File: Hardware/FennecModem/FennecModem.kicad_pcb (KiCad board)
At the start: 2 copper layers, 70 x 116.7 mm, 15 parts, among them J101 USB_C_Receptacle_USB2.0, J201 Conn_Coaxial, U101 ATmega32U4-A, U201 DRA818V

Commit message: Add more
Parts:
- moved FL201 83.8 mm to (150.5, 52.5), turned to 90 degrees
- moved J201 57.1 mm to (150.5, 42.9), turned to 90 degrees
- moved U201 49.2 mm to (164.0, 69.5), turned to -90 degrees
- moved J101 38.9 mm to (128.0, 45.0), turned to 180 degrees
- moved R204 37.8 mm to (151.0, 98.4)
- moved JP201 24.4 mm to (150.3, 84.0), turned to -90 degrees
- moved U101 14.3 mm to (151.0, 126.0), turned to 45 degrees
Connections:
- C101 pad 1: unconnected-(C101-Pad1) -> +5V
- C101 pad 15: unconnected-(C101-Pad15) -> GND
- C101 pad 16: unconnected-(C101-Pad16) -> +12V
- C101 pad 30: unconnected-(C101-Pad30) -> GND
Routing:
- net GND: track 0.00 -> 9.28 mm, vias 0 -> 35
- added copper zone on B.Cu, net GND
- added copper zone on F.Cu, net GND

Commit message: Bump kenwoodfox libs
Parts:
- moved J101 0.62 mm to (128.0, 44.4)
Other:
- board size 70 x 116.7 mm -> 75 x 116.7 mm

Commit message: Bump upstream libs with new logo
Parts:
- added G***: LOGO, KenwoodFox:fennec_logo, F.Cu at (174.5, 133.5)
- added G***: LOGO, KenwoodFox:fennec_logo, B.Cu at (125.0, 61.8)
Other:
- board text added: "F.E.N.N.E.C. MODEM"

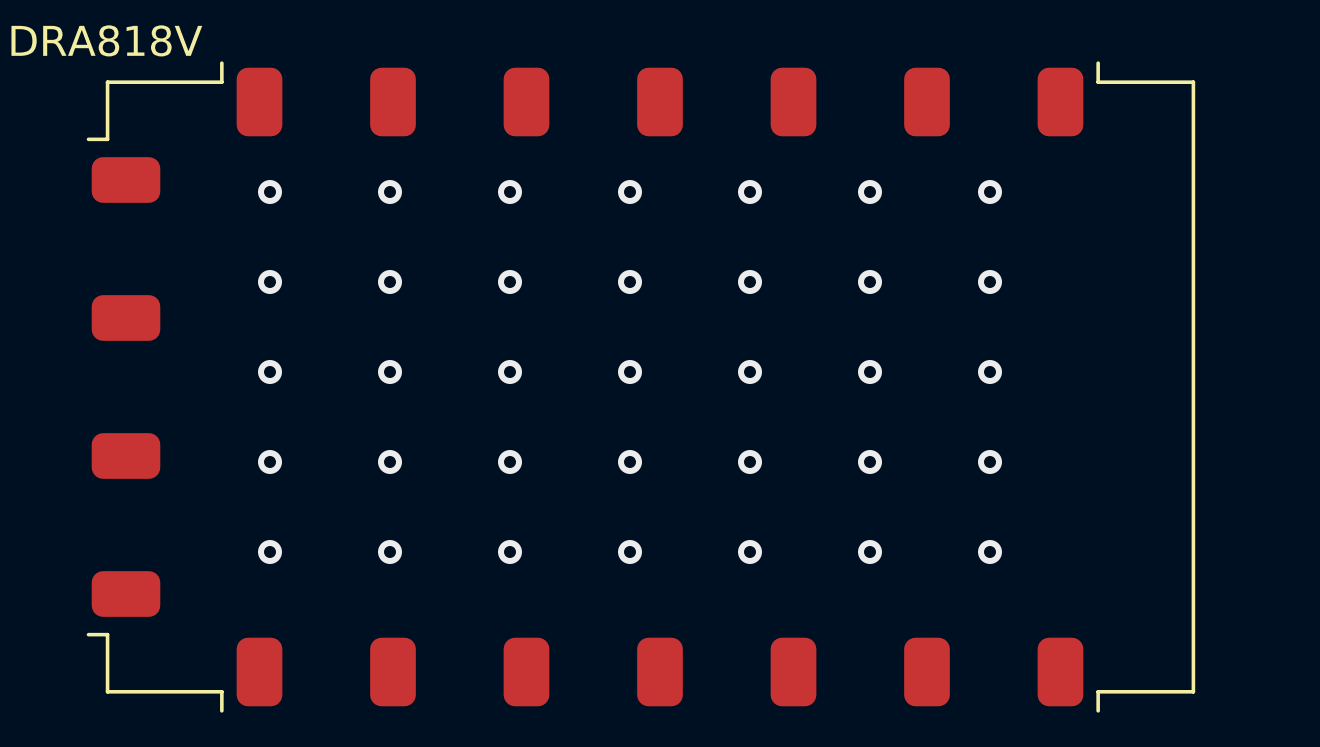
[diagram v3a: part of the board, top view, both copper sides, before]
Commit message: Bump kicad libs and add thermal holes to board
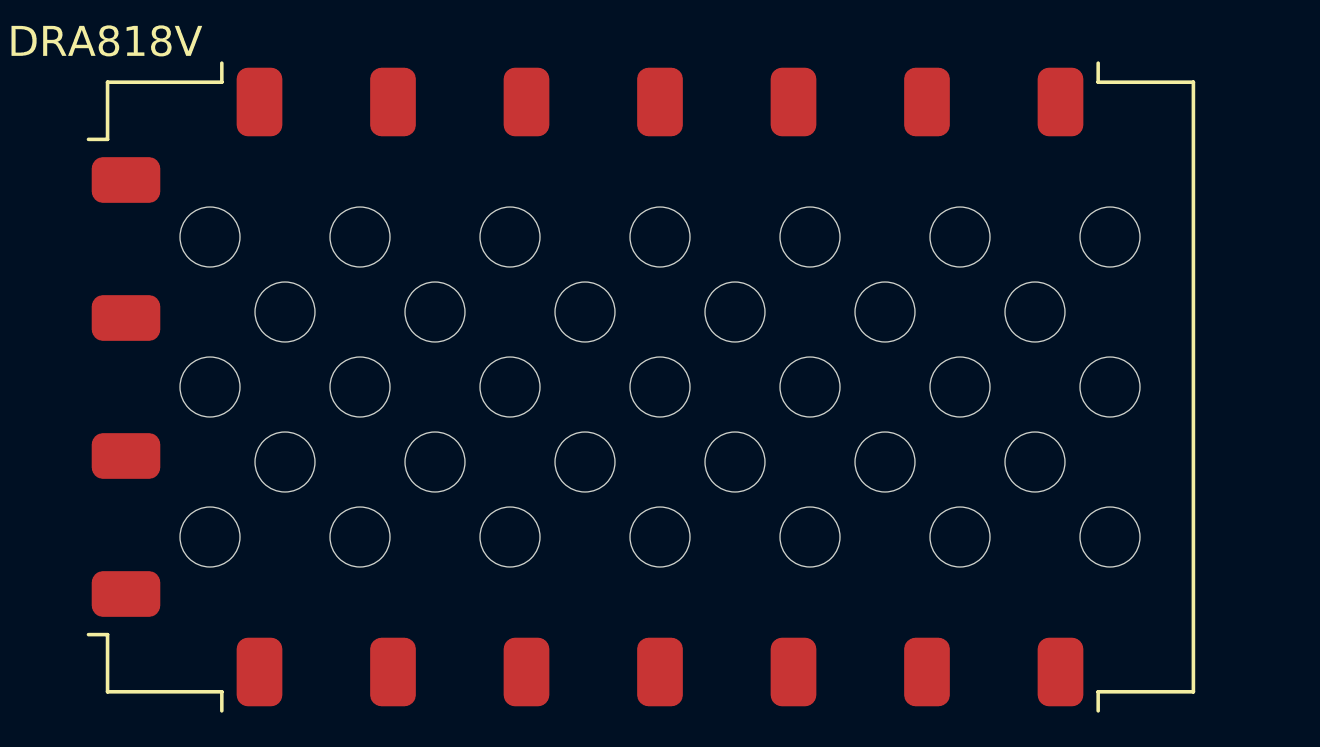
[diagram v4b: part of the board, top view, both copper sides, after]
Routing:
- net GND: vias 35 -> 0
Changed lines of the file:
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@@
         (effects (font (size 1 1) (thickness 0.15)))
     )
-    (fp_text user "${REFERENCE}" (at 0 0 unlocked) (layer "F.Fab")
+    (fp_text user "${REFERENCE}" (at 8.255 20.955 -90 unlocked) (layer "F.Fab")
         (effects (font (size 1 1) (thickness 0.15)))
     )
@@
     (fp_rect (start -9.525 -17.78) (end 9.525 17.78)
       (stroke (width 0.12) (type solid)) (fill none) (layer "F.Fab"))
+    (pad "" np_thru_hole circle (at -5 -15 270) (size 2 2) (drill 2) (layers "F&B.Cu" "*.Mask"))
+    (pad "" np_thru_hole circle (at -5 -10 270) (size 2 2) (drill 2) (layers "F&B.Cu" "*.Mask"))
+    (pad "" np_thru_hole circle (at -5 -5 270) (size 2 2) (drill 2) (layers "F&B.Cu" "*.Mask"))
+    (pad "" np_thru_hole circle (at -5 0 270) (size 2 2) (drill 2) (layers "F&B.Cu" "*.Mask"))
+    (pad "" np_thru_hole circle (at -5 5 270) (size 2 2) (drill 2) (layers "F&B.Cu" "*.Mask"))
+    (pad "" np_thru_hole circle (at -5 10 270) (size 2 2) (drill 2) (layers "F&B.Cu" "*.Mask"))
+    (pad "" np_thru_hole circle (at -5 15 270) (size 2 2) (drill 2) (layers "F&B.Cu" "*.Mask"))
+    (pad "" np_thru_hole circle (at -2.5 -12.5 270) (size 2 2) (drill 2) (layers "F&B.Cu" "*.Mask"))
+    (pad "" np_thru_hole circle (at -2.5 -7.5 270) (size 2 2) (drill 2) (layers "F&B.Cu" "*.Mask"))
+    (pad "" np_thru_hole circle (at -2.5 -2.5 270) (size 2 2) (drill 2) (layers "F&B.Cu" "*.Mask"))
+    (pad "" np_thru_hole circle (at -2.5 2.5 270) (size 2 2) (drill 2) (layers "F&B.Cu" "*.Mask"))
+    (pad "" np_thru_hole circle (at -2.5 7.5 270) (size 2 2) (drill 2) (layers "F&B.Cu" "*.Mask"))
+    (pad "" np_thru_hole circle (at -2.5 12.5 270) (size 2 2) (drill 2) (layers "F&B.Cu" "*.Mask"))
+    (pad "" np_thru_hole circle (at 0 -15 270) (size 2 2) (drill 2) (layers "F&B.Cu" "*.Mask"))
+    (pad "" np_thru_hole circle (at 0 -10 270) (size 2 2) (drill 2) (layers "F&B.Cu" "*.Mask"))
+    (pad "" np_thru_hole circle (at 0 -5 270) (size 2 2) (drill 2) (layers "F&B.Cu" "*.Mask"))
+    (pad "" np_thru_hole circle (at 0 0 270) (size 2 2) (drill 2) (layers "F&B.Cu" "*.Mask"))
+    (pad "" np_thru_hole circle (at 0 5 270) (size 2 2) (drill 2) (layers "F&B.Cu" "*.Mask"))
+    (pad "" np_thru_hole circle (at 0 10 270) (size 2 2) (drill 2) (layers "F&B.Cu" "*.Mask"))
+    (pad "" np_thru_hole circle (at 0 15 270) (size 2 2) (drill 2) (layers "F&B.Cu" "*.Mask"))
+    (pad "" np_thru_hole circle (at 2.5 -12.5 270) (size 2 2) (drill 2) (layers "F&B.Cu" "*.Mask"))
+    (pad "" np_thru_hole circle (at 2.5 -7.5 270) (size 2 2) (drill 2) (layers "F&B.Cu" "*.Mask"))
+    (pad "" np_thru_hole circle (at 2.5 -2.5 270) (size 2 2) (drill 2) (layers "F&B.Cu" "*.Mask"))
+    (pad "" np_thru_hole circle (at 2.5 2.5 270) (size 2 2) (drill 2) (layers "F&B.Cu" "*.Mask"))
+    (pad "" np_thru_hole circle (at 2.5 7.5 270) (size 2 2) (drill 2) (layers "F&B.Cu" "*.Mask"))
+    (pad "" np_thru_hole circle (at 2.5 12.5 270) (size 2 2) (drill 2) (layers "F&B.Cu" "*.Mask"))
+    (pad "" np_thru_hole circle (at 5 -15 270) (size 2 2) (drill 2) (layers "F&B.Cu" "*.Mask"))
+    (pad "" np_thru_hole circle (at 5 -10 270) (size 2 2) (drill 2) (layers "F&B.Cu" "*.Mask"))
+    (pad "" np_thru_hole circle (at 5 -5 270) (size 2 2) (drill 2) (layers "F&B.Cu" "*.Mask"))
+    (pad "" np_thru_hole circle (at 5 0 270) (size 2 2) (drill 2) (layers "F&B.Cu" "*.Mask"))
+    (pad "" np_thru_hole circle (at 5 5 270) (size 2 2) (drill 2) (layers "F&B.Cu" "*.Mask"))
+    (pad "" np_thru_hole circle (at 5 10 270) (size 2 2) (drill 2) (layers "F&B.Cu" "*.Mask"))
+    (pad "" np_thru_hole circle (at 5 15 270) (size 2 2) (drill 2) (layers "F&B.Cu" "*.Mask"))
     (pad "1" smd roundrect (at 9.5 -13.35 270) (size 2.286 1.524) (layers "F.Cu" "F.Mask") (roundrect_rratio 0.25)
       (net 30 "SQL") (pinfunction "SQ") (pintype "output"))
@@
   )
   (segment (start 150 154) (end 150 149.5) (width 2) (layer "F.Cu") (net 29))
-  (via (at 151 69) (size 0.8) (drill 0.4) (layers "F.Cu" "B.Cu") (free) (net 29))
-  (via (at 155 66) (size 0.8) (drill 0.4) (layers "F.Cu" "B.Cu") (free) (net 29))
-  (via (at 175 63) (size 0.8) (drill 0.4) (layers "F.Cu" "B.Cu") (free) (net 29))
-  (via (at 151 75) (size 0.8) (drill 0.4) (layers "F.Cu" "B.Cu") (free) (net 29))
-  (via (at 171 63) (size 0.8) (drill 0.4) (layers "F.Cu" "B.Cu") (free) (net 29))
-  (via (at 159 72) (size 0.8) (drill 0.4) (layers "F.Cu" "B.Cu") (free) (net 29))
-  (via (at 175 69) (size 0.8) (drill 0.4) (layers "F.Cu" "B.Cu") (free) (net 29))
-  (via (at 171 69) (size 0.8) (drill 0.4) (layers "F.Cu" "B.Cu") (free) (net 29))
-  (via (at 155 75) (size 0.8) (drill 0.4) (layers "F.Cu" "B.Cu") (free) (net 29))
-  (via (at 175 66) (size 0.8) (drill 0.4) (layers "F.Cu" "B.Cu") (free) (net 29))
-  (via (at 167 72) (size 0.8) (drill 0.4) (layers "F.Cu" "B.Cu") (free) (net 29))
-  (via (at 167 66) (size 0.8) (drill 0.4) (layers "F.Cu" "B.Cu") (free) (net 29))
-  (via (at 151 66) (size 0.8) (drill 0.4) (layers "F.Cu" "B.Cu") (free) (net 29))
-  (via (at 155 63) (size 0.8) (drill 0.4) (layers "F.Cu" "B.Cu") (free) (net 29))
-  (via (at 171 66) (size 0.8) (drill 0.4) (layers "F.Cu" "B.Cu") (free) (net 29))
-  (via (at 159 63) (size 0.8) (drill 0.4) (layers "F.Cu" "B.Cu") (free) (net 29))
-  (via (at 163 66) (size 0.8) (drill 0.4) (layers "F.Cu" "B.Cu") (free) (net 29))
-  (via (at 167 63) (size 0.8) (drill 0.4) (layers "F.Cu" "B.Cu") (free) (net 29))
-  (via (at 151 63) (size 0.8) (drill 0.4) (layers "F.Cu" "B.Cu") (free) (net 29))
-  (via (at 171 72) (size 0.8) (drill 0.4) (layers "F.Cu" "B.Cu") (free) (net 29))
-  (via (at 163 69) (size 0.8) (drill 0.4) (layers "F.Cu" "B.Cu") (free) (net 29))
-  (via (at 175 75) (size 0.8) (drill 0.4) (layers "F.Cu" "B.Cu") (free) (net 29))
-  (via (at 159 69) (size 0.8) (drill 0.4) (layers "F.Cu" "B.Cu") (free) (net 29))
-  (via (at 155 72) (size 0.8) (drill 0.4) (layers "F.Cu" "B.Cu") (free) (net 29))
-  (via (at 163 63) (size 0.8) (drill 0.4) (layers "F.Cu" "B.Cu") (free) (net 29))
-  (via (at 167 69) (size 0.8) (drill 0.4) (layers "F.Cu" "B.Cu") (free) (net 29))
-  (via (at 167 75) (size 0.8) (drill 0.4) (layers "F.Cu" "B.Cu") (free) (net 29))
-  (via (at 159 66) (size 0.8) (drill 0.4) (layers "F.Cu" "B.Cu") (free) (net 29))
-  (via (at 171 75) (size 0.8) (drill 0.4) (layers "F.Cu" "B.Cu") (free) (net 29))
-  (via (at 175 72) (size 0.8) (drill 0.4) (layers "F.Cu" "B.Cu") (free) (net 29))
-  (via (at 155 69) (size 0.8) (drill 0.4) (layers "F.Cu" "B.Cu") (free) (net 29))
-  (via (at 163 72) (size 0.8) (drill 0.4) (layers "F.Cu" "B.Cu") (free) (net 29))
-  (via (at 151 72) (size 0.8) (drill 0.4) (layers "F.Cu" "B.Cu") (free) (net 29))
-  (via (at 159 75) (size 0.8) (drill 0.4) (layers "F.Cu" "B.Cu") (free) (net 29))
-  (via (at 163 75) (size 0.8) (drill 0.4) (layers "F.Cu" "B.Cu") (free) (net 29))
   (segment (start 177.72 154) (end 177.72 149.22) (width 2) (layer "B.Cu") (net 29))
   (zone (net 29) (net_name "GND") (layers "F&B.Cu") (hatch edge 0.508)

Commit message: Bump all pcb
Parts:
- removed JP201: H/L Jumper, Connector_PinHeader_2.54mm:PinHeader_1x02_P2.54mm_Vertical
- added D203: TX, LED_SMD:LED_0805_2012Metric, F.Cu at (206.5, 42.4)
- added D204: TXD, LED_SMD:LED_0805_2012Metric, F.Cu at (200.8, 42.4)
- added G***: LOGO, KenwoodFox:KITSUNE_LOGO, F.Cu at (176.2, 47.0)
- added R205: 300, Resistor_SMD:R_0805_2012Metric, F.Cu at (206.5, 46.4)
- added R206: 47R, Resistor_SMD:R_0805_2012Metric, F.Cu at (166.1, 118.8)
- added REF**: KiCad-Logo2_5mm_SilkScreen, Symbol:KiCad-Logo2_5mm_SilkScreen, F.Cu at (163.2, 48.8)
- added REF**: OSHW-Logo2_7.3x6mm_SilkScreen, Symbol:OSHW-Logo2_7.3x6mm_SilkScreen, F.Cu at (166.0, 43.5)
- D201: footprint LED_SMD:LED_0603_1608Metric -> LED_SMD:LED_0805_2012Metric
- D202: value TX -> RXD; footprint LED_SMD:LED_0603_1608Metric -> LED_SMD:LED_0805_2012Metric
- G***: moved to F.Cu
- G***: moved to B.Cu
- R204: value 47R -> 300
- moved G*** 87.2 mm to (125.0, 61.7), turned to 180 degrees
- moved R202 82.2 mm to (209.2, 46.4), turned to -90 degrees
- moved D201 80.3 mm to (209.2, 42.4), turned to -90 degrees
- moved R204 71.9 mm to (200.8, 46.4), turned to -90 degrees
- moved R203 60.6 mm to (203.8, 46.4), turned to -90 degrees
- moved D202 59.2 mm to (203.8, 42.4), turned to -90 degrees
- moved C201 23.2 mm to (161.7, 115.8)
- moved R201 13.3 mm to (166.1, 115.8)
- moved C202 12.2 mm to (161.7, 118.8)
- moved U201 5.75 mm to (164.0, 63.8)
- moved FL201 3.00 mm to (150.5, 49.5)
- turned G*** to 0 degrees
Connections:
- net Net-(R201-Pad1) renamed /Radio/Sleep
- net SQL renamed /Radio/SQL
- D202 pad 1: PTT -> /Radio/RXD
- D202 pad 2: Net-(D202-Pad2) -> Net-(D202-A)
- R203 pad 1: +5V -> Net-(D202-A)
- R203 pad 2: Net-(D202-Pad2) -> +5V
- R204 pad 1: PTT -> Net-(D204-A)
- R204 pad 2: PTT -> +5V
- U201 pad 5: PTT -> Net-(U201-PTT)
- U201 pad 7: H/L -> /Radio/H/L
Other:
- board text added: "${COMMENT1}"
- board text added: "${FULL_REVISION}"

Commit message: Add fennec modem pieces
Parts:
- added C102: 22pf, Capacitor_SMD:C_0805_2012Metric, F.Cu at (176.3, 133.4)
- added C103: 22pf, Capacitor_SMD:C_0805_2012Metric, F.Cu at (176.3, 130.4)
- added R101: 300, Resistor_SMD:R_0805_2012Metric, F.Cu at (171.9, 133.4)
- added R102: 300, Resistor_SMD:R_0805_2012Metric, F.Cu at (171.9, 130.4)
- added Y101: 16mHz, Crystal:Crystal_SMD_HC49-SD, F.Cu at (163.5, 137.0)
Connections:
- J101 pad A6: unconnected-(J101-D+-PadA6) -> /D+
- J101 pad A7: unconnected-(J101-D--PadA7) -> /D-
- J101 pad B6: unconnected-(J101-D+-PadB6) -> /D+
- J101 pad B7: unconnected-(J101-D--PadB7) -> /D-
- U101 pad 16: unconnected-(U101-XTAL2-Pad16) -> Net-(U101-XTAL2)
- U101 pad 17: unconnected-(U101-XTAL1-Pad17) -> Net-(U101-XTAL1)
- U101 pad 3: unconnected-(U101-D--Pad3) -> Net-(U101-D-)
- U101 pad 4: unconnected-(U101-D+-Pad4) -> Net-(U101-D+)

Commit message: Bump modem
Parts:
- added D101: STAT, LED_THT:LED_D3.0mm_Horizontal_O1.27mm_Z2.0mm, B.Cu at (149.0, 44.0)
- added R103: 300, Resistor_SMD:R_0805_2012Metric, F.Cu at (144.5, 48.6)
- D201, D203: footprint LED_SMD:LED_0805_2012Metric -> LED_THT:LED_D3.0mm_Horizontal_O1.27mm_Z2.0mm; moved to B.Cu
- moved D203 68.6 mm to (138.0, 44.0), turned to 0 degrees
- moved D202 67.5 mm to (180.9, 106.0), turned to 180 degrees
- moved R202 66.8 mm to (142.5, 48.6)
- moved R205 66.0 mm to (140.5, 48.6)
- moved D201 65.8 mm to (143.5, 44.0), turned to 0 degrees
- moved R203 65.3 mm to (176.9, 106.0), turned to 180 degrees
- moved D204 63.7 mm to (180.9, 103.0), turned to 180 degrees
- moved R204 61.4 mm to (176.9, 103.0), turned to 180 degrees
- moved G*** 28.6 mm to (178.8, 75.5), turned to -90 degrees
- moved REF** 27.2 mm to (182.2, 65.2), turned to -90 degrees
- moved J201 22.8 mm to (173.2, 42.5)
- moved FL201 22.6 mm to (173.1, 49.0)
- moved REF** 19.4 mm to (177.0, 62.5), turned to -90 degrees
- moved U201 6.47 mm to (160.8, 69.3), turned to 180 degrees
